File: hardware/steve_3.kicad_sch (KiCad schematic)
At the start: 22 parts, among them J2 Screw_Terminal_01x04, U2 TI_TPS51386RJNR_Regulator_Buc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

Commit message: Added buzzer and LEDs to schematic
Added buzzer and LEDs (4 regular and 2 WS2812B) to schematic. Minor schematic fixes such as PMIC enable pin voltage divider.
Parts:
- removed R8: 200k, Resistor_SMD:R_0603_1608Metric, symbol Device:R_US
- R10: value 120k -> 100k 1%
- R4, R6: value 0k -> 0k 1%
- R5: value 20k -> 20k 1%
- R7: value 150k -> 150k 1%
- R9: value 200k -> 330k 1%
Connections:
- net +BATT: now also R9.1
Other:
- moved on the sheet: R10, R9
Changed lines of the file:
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@@
 	)
 	(junction
-		(at 273.05 46.99)
+		(at 271.78 49.53)
 		(diameter 0)
 		(color 0 0 0 0)
@@
 	(wire
 		(pts
-			(xy 273.05 57.15) (xy 273.05 59.69)
+			(xy 271.78 59.69) (xy 271.78 63.5)
 		)
 		(stroke
@@
 	(wire
 		(pts
-			(xy 273.05 46.99) (xy 273.05 49.53)
+			(xy 271.78 49.53) (xy 271.78 52.07)
 		)
 		(stroke
@@
 	(wire
 		(pts
-			(xy 273.05 34.29) (xy 273.05 36.83)
+			(xy 271.78 35.56) (xy 271.78 39.37)
 		)
 		(stroke
@@
 	(wire
 		(pts
-			(xy 269.24 46.99) (xy 273.05 46.99)
+			(xy 267.97 49.53) (xy 271.78 49.53)
 		)
 		(stroke
@@
 	(wire
 		(pts
-			(xy 273.05 24.13) (xy 273.05 26.67)
-		)
-		(stroke
-			(width 0)
-			(type default)
-		)
-	)
-	(wire
-		(pts
 			(xy 26.67 86.36) (xy 26.67 82.55)
 		)
@@
 	(wire
 		(pts
-			(xy 273.05 44.45) (xy 273.05 46.99)
+			(xy 271.78 46.99) (xy 271.78 49.53)
 		)
 		(stroke
@@
 		)
 	)
-	(text_box ""
+	(text_box "Voltage divider for the 5V regulator enable pin.\nThe enable pin has an absolute max voltage of 6V (see Section 6.1).\nThe enable threshold high level must be at least 1.31V (see Section 6.5).\nThese R values were chosen so that the enable pin voltage is ~23% (100/(330+100)) of +BATT.\nThis allows a fully charged 6s LiPo battery to safely enable the regulator (25.2V * .23256 = 5.86V).\nThis also allows a 2s LiPo battery at a low state of charge (~3V per cell)\nto still enable the regulator (6V * .23256 = 1.39V)."
 		(exclude_from_sim no)
-		(at 64.77 20.32 0)
-		(size 0 0)
+		(at 234.95 26.67 0)
+		(size 33.02 16.51)
 		(stroke
 			(width 0)
@@
 		)
 	)
-	(text_box "Assuming that SS can be left floating if the default start time is acceptable"
+	(text_box ""
 		(exclude_from_sim no)
-		(at 64.77 39.37 0)
-		(size 16.51 5.08)
+		(at 64.77 20.32 0)
+		(size 0 0)
 		(stroke
 			(width 0)
@@
 		)
 	)
-	(text_box "Voltage divider for the 5V regulator enable pin.\nThe enable pin has an absolute max voltage of 6V (see Section 6.1).\nThe enable threshold high level must be at least 1.31V (see Section 6.5).\nThese R values were chosen so that the enable pin voltage is ~23% (120/520) of +BATT.\nThis allows a fully charged 6s LiPo battery to safely enable the regulator (25.2V * .23 = 5.8V).\nThis also allows a 2s LiPo battery at a low state of charge (~3V per cell)\nto still enable the regulator (6V * .23 = 1.38V)."
+	(text_box "Assuming that SS can be left floating if the default start time is acceptable"
 		(exclude_from_sim no)
-		(at 238.76 21.59 0)
-		(size 31.75 16.51)
+		(at 64.77 39.37 0)
+		(size 16.51 5.08)
 		(stroke
 			(width 0)
@@
 	(global_label "U2_EN"
 		(shape input)
-		(at 269.24 46.99 180)
+		(at 267.97 49.53 180)
 		(fields_autoplaced yes)
 		(effects
@@
 		)
 		(property "Intersheetrefs" "${INTERSHEET_REFS}"
-			(at 260.2677 46.99 0)
+			(at 258.9977 49.53 0)
 			(effects
 				(font
@@
 		(dnp no)
 		(property "Reference" "R5"
-			(at 152.654 57.15 0)
+			(at 159.512 60.96 0)
 			(effects
 				(font
@@
 			)
 		)
-		(property "Value" "20k"
-			(at 152.654 64.008 0)
+		(property "Value" "20k 1%"
+			(at 157.988 63.754 0)
 			(effects
 				(font
@@
 			)
 		)
-		(property "Value" "0k"
-			(at 156.718 37.084 90)
+		(property "Value" "0k 1%"
+			(at 155.194 41.656 90)
 			(effects
 				(font
@@
 	)
 	(symbol
-		(lib_id "Device:R_US")
-		(at 273.05 30.48 0)
-		(unit 1)
-		(exclude_from_sim no)
-		(in_bom yes)
-		(on_board yes)
-		(dnp no)
-		(fields_autoplaced yes)
-		(property "Reference" "R8"
-			(at 275.59 29.2099 0)
-			(effects
-				(font
-					(size 1.27 1.27)
-				)
-				(justify left)
-			)
-		)
-		(property "Value" "200k"
-			(at 275.59 31.7499 0)
-			(effects
-				(font
-					(size 1.27 1.27)
-				)
-				(justify left)
-			)
-		)
-		(property "Footprint" "Resistor_SMD:R_0603_1608Metric"
-			(at 274.066 30.734 90)
-			(effects
-				(font
-					(size 1.27 1.27)
-				)
-				(hide yes)
-			)
-		)
-		(property "Datasheet" "~"
-			(at 273.05 30.48 0)
-			(effects
-				(font
-					(size 1.27 1.27)
-				)
-				(hide yes)
-			)
-		)
-		(property "Description" "Resistor, US symbol"
-			(at 273.05 30.48 0)
-			(effects
-				(font
-					(size 1.27 1.27)
-				)
-				(hide yes)
-			)
-		)
-		(pin "2"
-		)
-		(pin "1"
-		)
-		(instances
-			(project "steve"
-				(path "/f7ed98e3-ddd9-4c0c-9e06-df5f86e74283/203efb9b-0e38-445a-a51a-cbb7d642002b"
-					(reference "R8")
-					(unit 1)
-				)
-			)
-		)
-	)
-	(symbol
 		(lib_id "Imported_Symbols:TI_TPS51386RJNR_Regulator_Buck_8A")
 		(at 82.55 29.21 0)
@@
 	(symbol
 		(lib_id "power:+BATT")
-		(at 273.05 24.13 0)
+		(at 271.78 35.56 0)
 		(unit 1)
 		(exclude_from_sim no)
@@
 		(fields_autoplaced yes)
 		(property "Reference" "#PWR041"
-			(at 273.05 27.94 0)
+			(at 271.78 39.37 0)
 			(effects
 				(font
@@
 		)
 		(property "Value" "+BATT"
-			(at 273.05 19.05 0)
+			(at 271.78 30.48 0)
 			(effects
 				(font
@@
 		)
 		(property "Footprint" ""
-			(at 273.05 24.13 0)
+			(at 271.78 35.56 0)
 			(effects
 				(font
@@
 		)
 		(property "Datasheet" ""
-			(at 273.05 24.13 0)
+			(at 271.78 35.56 0)
 			(effects
 				(font
@@
 		)
 		(property "Description" "Power symbol creates a global label with name \"+BATT\""
-			(at 273.05 24.13 0)
+			(at 271.78 35.56 0)
 			(effects
 				(font
@@
 	(symbol
 		(lib_id "power:GND")
-		(at 273.05 59.69 0)
+		(at 271.78 63.5 0)
 		(unit 1)
 		(exclude_from_sim no)
@@
 		(dnp no)
 		(property "Reference" "#PWR042"
-			(at 273.05 66.04 0)
+			(at 271.78 69.85 0)
 			(effects
 				(font
@@
 		)
 		(property "Value" "GND"
-			(at 275.844 59.436 0)
+			(at 274.574 63.246 0)
 			(effects
 				(font
@@
 		)
 		(property "Footprint" ""
-			(at 273.05 59.69 0)
+			(at 271.78 63.5 0)
 			(effects
 				(font
@@
 		)
 		(property "Datasheet" ""
-			(at 273.05 59.69 0)
+			(at 271.78 63.5 0)
 			(effects
 				(font
@@
 		)
 		(property "Description" "Power symbol creates a global label with name \"GND\" , ground"
-			(at 273.05 59.69 0)
+			(at 271.78 63.5 0)
 			(effects
 				(font
@@
 	(symbol
 		(lib_id "Device:R_US")
-		(at 273.05 40.64 0)
+		(at 271.78 43.18 0)
 		(unit 1)
 		(exclude_from_sim no)
@@
 		(fields_autoplaced yes)
 		(property "Reference" "R9"
-			(at 275.59 39.3699 0)
+			(at 274.32 41.9099 0)
 			(effects
 				(font
@@
 			)
 		)
-		(property "Value" "200k"
-			(at 275.59 41.9099 0)
+		(property "Value" "330k 1%"
+			(at 274.32 44.4499 0)
 			(effects
 				(font
@@
 		)
 		(property "Footprint" "Resistor_SMD:R_0603_1608Metric"
-			(at 274.066 40.894 90)
+			(at 272.796 43.434 90)
 			(effects
 				(font
@@
 		)
 		(property "Datasheet" "~"
-			(at 273.05 40.64 0)
+			(at 271.78 43.18 0)
 			(effects
 				(font
@@
 		)
 		(property "Description" "Resistor, US symbol"
-			(at 273.05 40.64 0)
+			(at 271.78 43.18 0)
 			(effects
 				(font
@@
 		(dnp no)
 		(property "Reference" "R7"
-			(at 178.816 48.006 90)
+			(at 186.69 48.26 90)
 			(effects
 				(font
@@
 			)
 		)
-		(property "Value" "150k"
-			(at 187.706 47.752 90)
+		(property "Value" "150k 1%"
+			(at 176.022 48.26 90)
 			(effects
 				(font
@@
 		(dnp no)
 		(property "Reference" "R6"
-			(at 164.846 57.15 90)
+			(at 167.64 52.07 90)
 			(effects
 				(font
@@
 			)
 		)
-		(property "Value" "0k"
-			(at 171.196 56.642 90)
+		(property "Value" "0k 1%"
+			(at 167.894 57.404 90)
 			(effects
 				(font
@@
 	(symbol
 		(lib_id "Device:R_US")
-		(at 273.05 53.34 0)
+		(at 271.78 55.88 0)
 		(unit 1)
 		(exclude_from_sim no)
@@
 		(fields_autoplaced yes)
 		(property "Reference" "R10"
-			(at 275.59 52.0699 0)
+			(at 274.32 54.6099 0)
 			(effects
 				(font
@@
 			)
 		)
-		(property "Value" "120k"
-			(at 275.59 54.6099 0)
+		(property "Value" "100k 1%"
+			(at 274.32 57.1499 0)
 			(effects
 				(font
@@
 		)
 		(property "Footprint" "Resistor_SMD:R_0603_1608Metric"
-			(at 274.066 53.594 90)
+			(at 272.796 56.134 90)
 			(effects
 				(font
@@
 		)
 		(property "Datasheet" "~"
-			(at 273.05 53.34 0)
+			(at 271.78 55.88 0)
 			(effects
 				(font
@@
 		)
 		(property "Description" "Resistor, US symbol"
-			(at 273.05 53.34 0)
+			(at 271.78 55.88 0)
 			(effects
 				(font

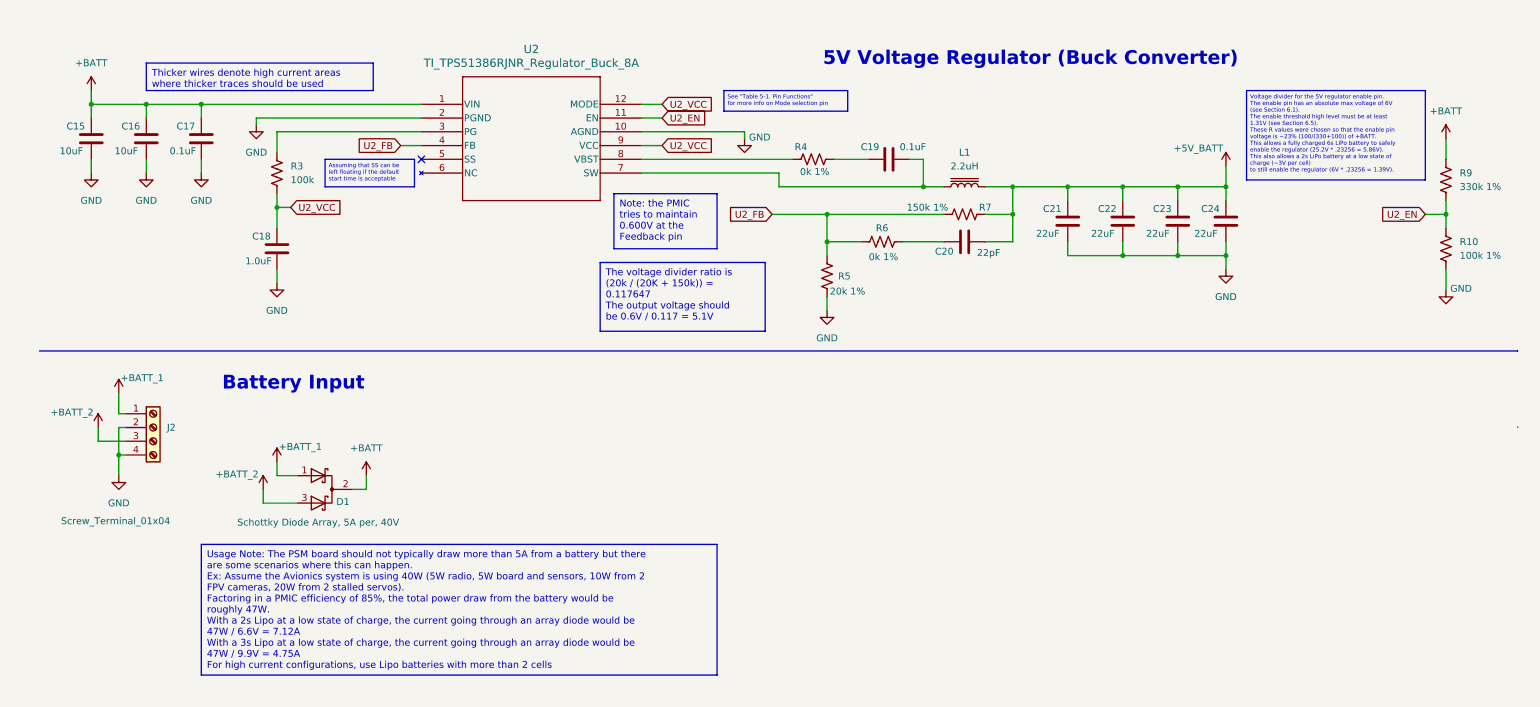
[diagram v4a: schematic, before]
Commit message: Removed PSM board components; added power conn; fixed telem conn
Moved PSM board components to the PSM board schematic.
Added a connector for the regulated 5V input to STEVE that comes from the PSM board.
Changed the radio telemetry connector to a 4 pin screwless terminal block to mitigate current limit concerns with the previous connector.
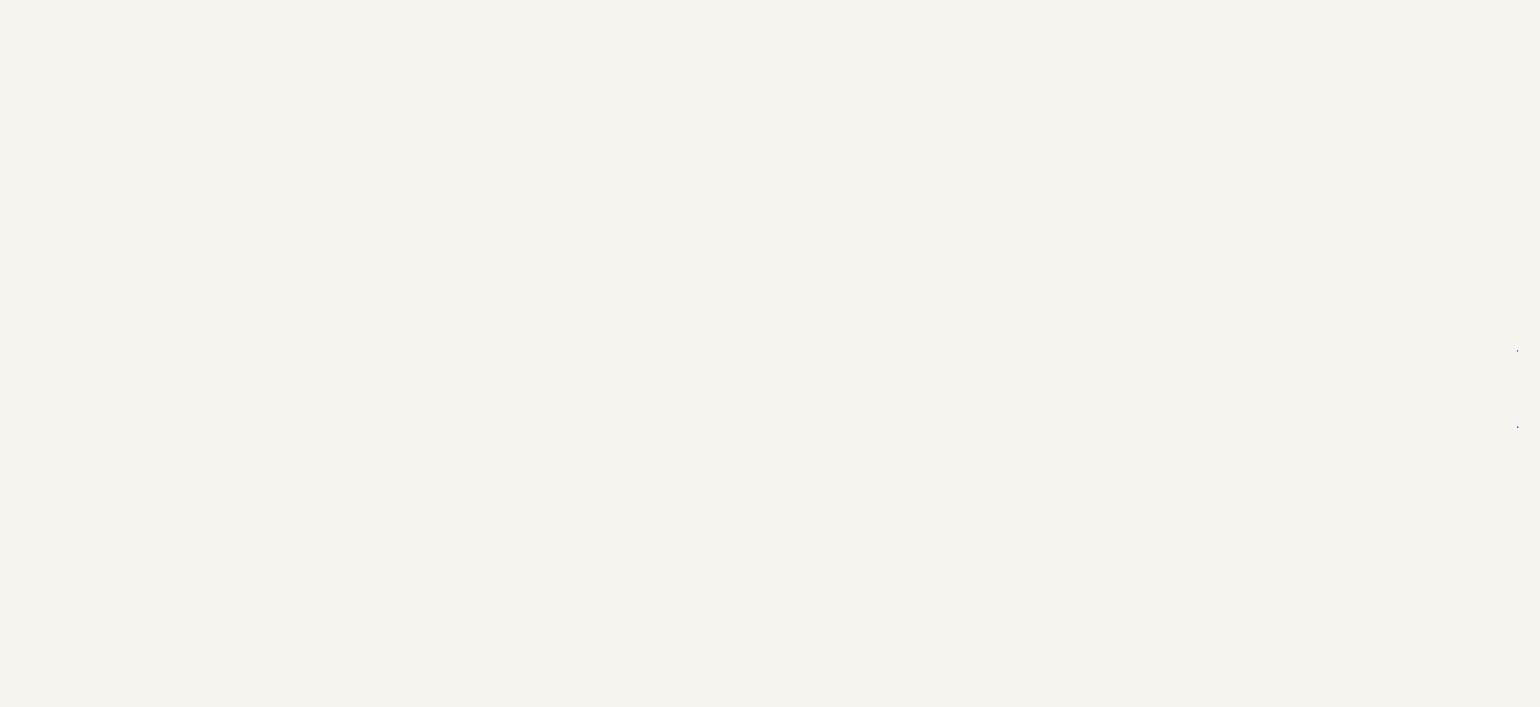
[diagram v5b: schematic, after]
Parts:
- removed C15, C16: 10uF, Capacitor_SMD:C_1206_3216Metric, symbol Device:C
- removed C17, C19: 0.1uF, Capacitor_SMD:C_0603_1608Metric, symbol Device:C
- removed C18: 1.0uF, Capacitor_SMD:C_0603_1608Metric, symbol Device:C
- removed C20: 22pF, Capacitor_SMD:C_0603_1608Metric, symbol Device:C
- removed C21, C22, C23, C24: 22uF, Capacitor_SMD:C_1206_3216Metric, symbol Device:C
- removed D1: Schottky Diode Array, 5A per, 40V, Imported_Footprints:PDS1040CTL-13_PowerDI-5, symbol Device:D_Schottky_Dual_CommonCathode_AKA_Parallel
- removed J2: Screw_Terminal_01x04, TerminalBlock_Phoenix:TerminalBlock_Phoenix_PT-1,5-4-5.0-H_1x04_P5.00mm_Horizontal, symbol Connector:Screw_Terminal_01x04
- removed L1: 2.2uH, Inductor_SMD:L_Coilcraft_XAL6060-XXX, symbol Device:L_Iron
- removed R10: 100k 1%, Resistor_SMD:R_0603_1608Metric, symbol Device:R_US
- removed R3: 100k, Resistor_SMD:R_0603_1608Metric, symbol Device:R_US
- removed R4, R6: 0k 1%, Resistor_SMD:R_0603_1608Metric, symbol Device:R_US
- removed R5: 20k 1%, Resistor_SMD:R_0603_1608Metric, symbol Device:R_US
- removed R7: 150k 1%, Resistor_SMD:R_0603_1608Metric, symbol Device:R_US
- removed R9: 330k 1%, Resistor_SMD:R_0603_1608Metric, symbol Device:R_US
- removed U2: TI_TPS51386RJNR_Regulator_Buck_8A, Imported_Footprints:TI_TPS51386RJNR_VQFN-HR_REG_BUCK_8A, symbol Imported_Symbols:TI_TPS51386RJNR_Regulator_Buck_8A
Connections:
- no-connect marks 1 -> 0
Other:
- note removed: "5V Voltage Regulator (Buck Converter)"
- note removed: "Battery Input"

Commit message: Finished schematic
Finished schematic - 3D model fixes using custom imports, all important parts sourced, additional GPIO/bus pins broken out, PSM board signals broken out, battery voltage sense line added.
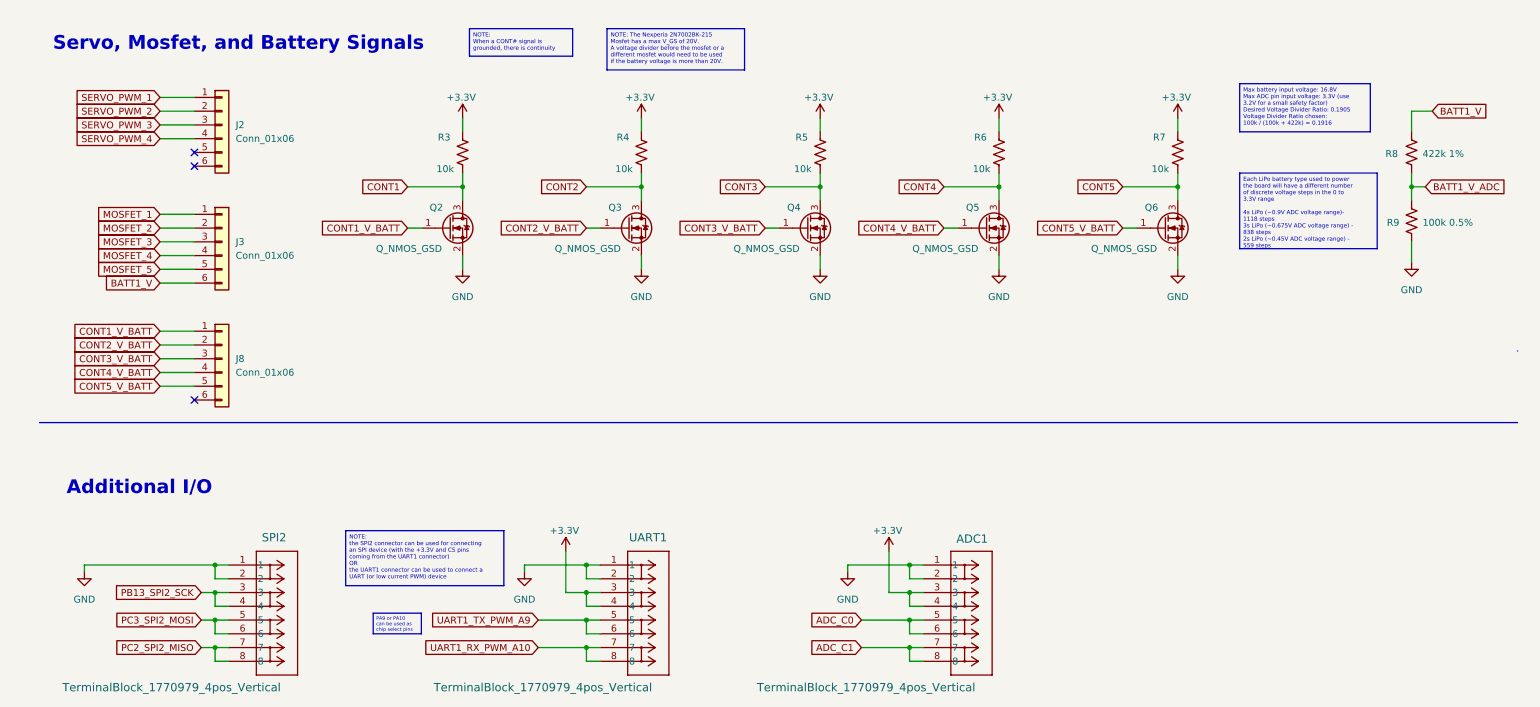
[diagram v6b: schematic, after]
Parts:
- added ADC1, SPI2, UART1: TerminalBlock_1770979_4pos_Vertical, Imported_Footprints:CONN_1814582_TerminalBlock_1770979_4pos_Vertical, symbol Imported_Symbols:TerminalBlock_1770979_4pos_Vertical
- added J2, J3, J8: Conn_01x06, Connector_JST:JST_GH_BM06B-GHS-TBT_1x06-1MP_P1.25mm_Vertical, symbol Connector_Generic:Conn_01x06
- added Q2, Q3, Q4, Q5, Q6: Q_NMOS_GSD, Package_TO_SOT_SMD:SOT-23, symbol Device:Q_NMOS_GSD
- added R3, R4, R5, R6, R7: 10k, Resistor_SMD:R_0603_1608Metric, symbol Device:R_US
- added R8: 422k 1%, Resistor_SMD:R_0603_1608Metric, symbol Device:R_US
- added R9: 100k 0.5%, Resistor_SMD:R_0603_1608Metric, symbol Device:R_US
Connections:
- new net +3.3V: ADC1.3, ADC1.4, R3.2, R4.2, R5.2, R6.2, R7.2, UART1.3, UART1.4
- new net ADC_C0: ADC1.5, ADC1.6
- new net ADC_C1: ADC1.7, ADC1.8
- new net BATT1_V: J3.6 (Pin_6), R8.2
- new net BATT1_V_ADC: R8.1, R9.2
- new net CONT1: Q2.3 (D), R3.1
- new net CONT1_V_BATT: J8.1 (Pin_1), Q2.1 (G)
- new net CONT2: Q3.3 (D), R4.1
- new net CONT2_V_BATT: J8.2 (Pin_2), Q3.1 (G)
- new net CONT3: Q4.3 (D), R5.1
- new net CONT3_V_BATT: J8.3 (Pin_3), Q4.1 (G)
- new net CONT4: Q5.3 (D), R6.1
- new net CONT4_V_BATT: J8.4 (Pin_4), Q5.1 (G)
- new net CONT5: Q6.3 (D), R7.1
- new net CONT5_V_BATT: J8.5 (Pin_5), Q6.1 (G)
- new net GND: ADC1.1, ADC1.2, Q2.2 (S), Q3.2 (S), Q4.2 (S), Q5.2 (S), Q6.2 (S), R9.1, SPI2.1, SPI2.2, UART1.1, UART1.2
- new net MOSFET_1: J3.1 (Pin_1)
- new net MOSFET_2: J3.2 (Pin_2)
- new net MOSFET_3: J3.3 (Pin_3)
- new net MOSFET_4: J3.4 (Pin_4)
- new net MOSFET_5: J3.5 (Pin_5)
- new net PB13_SPI2_SCK: SPI2.3, SPI2.4
- new net PC2_SPI2_MISO: SPI2.7, SPI2.8
- new net PC3_SPI2_MOSI: SPI2.5, SPI2.6
- new net SERVO_PWM_1: J2.1 (Pin_1)
- new net SERVO_PWM_2: J2.2 (Pin_2)
- new net SERVO_PWM_3: J2.3 (Pin_3)
- new net SERVO_PWM_4: J2.4 (Pin_4)
- new net UART1_RX_PWM_A10: UART1.7, UART1.8
- new net UART1_TX_PWM_A9: UART1.5, UART1.6
- no-connect marks 0 -> 3
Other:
- note added: "Additional I/O"
- note added: "Servo, Mosfet, and Battery Signals"

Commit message: started component layout
started component layout - attempting to use a 60x60mm board size
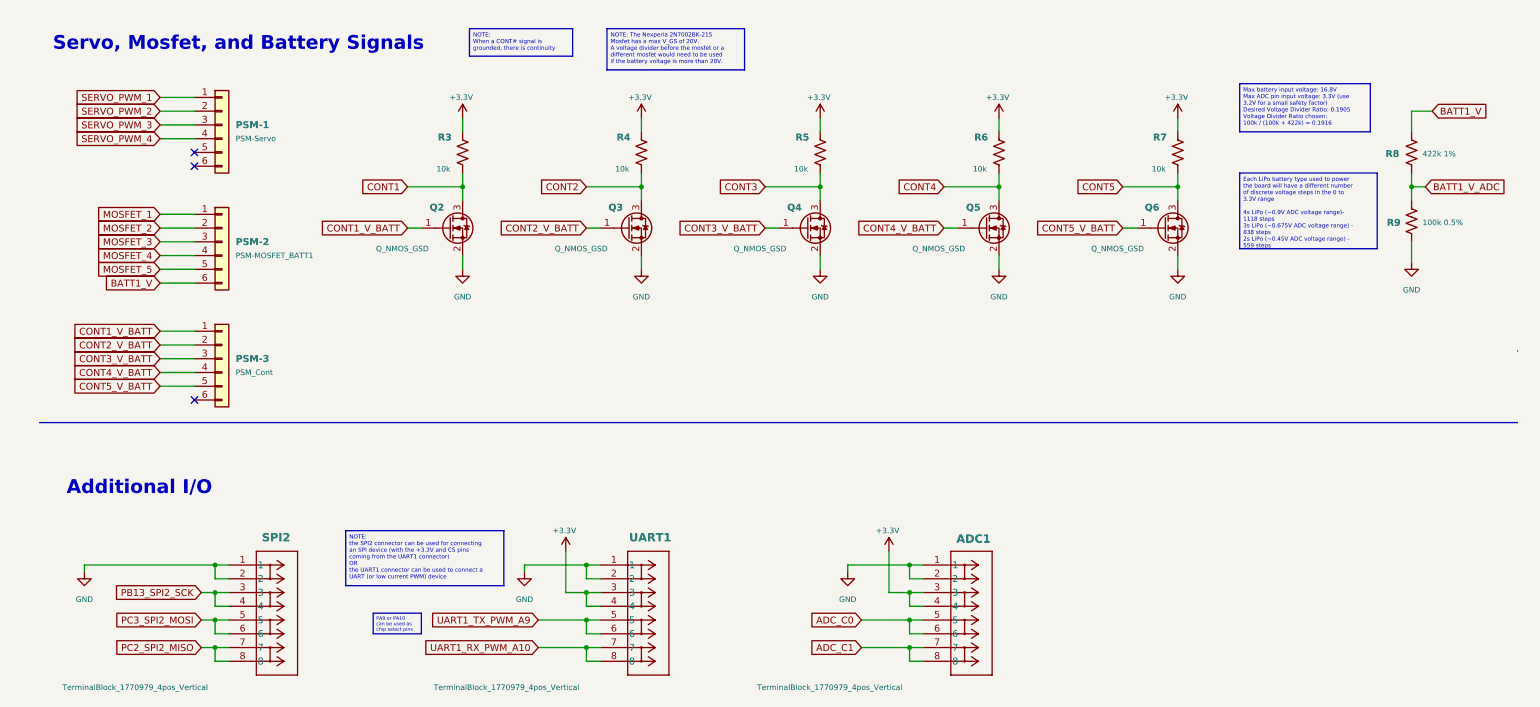
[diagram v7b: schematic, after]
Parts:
- PSM-1: renamed from J2; value Conn_01x06 -> PSM-Servo
- PSM-2: renamed from J3; value Conn_01x06 -> PSM-MOSFET_BATT1
- PSM-3: renamed from J8; value Conn_01x06 -> PSM_Cont
